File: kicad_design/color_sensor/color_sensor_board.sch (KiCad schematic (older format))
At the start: 5 parts, among them P1 CONN_6X2, P2 CONN_2, P3 CONN_2, U1 TCS3200

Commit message: Created new version 1.1 of the color sensor PCB. New version has a 5x2 header replacing the 6x2 header. Routed the shield board and re-routed sensor v1.1. Created gerber files.
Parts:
- removed P1: CONN_6X2, symbol CONN_6X2
- added P1: CONN_5X2, symbol CONN_5X2
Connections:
- net 5V: now also P1.1
- net GND: now also P1.3
- net A0 renamed S0
- net S0: now also P1.5
- net A1 renamed BLUE
- net BLUE: now also P1.6
- net A2 renamed GREEN
- net GREEN: now also P1.4
- net A3 renamed RED
- net RED: now also P1.2
- net D2 renamed FREQ
- net FREQ: now also P1.8
- net D3 renamed S2
- net S2: now also P1.9
- net D4 renamed S3
- net S3: now also P1.10
- net D5 renamed S1
- net S1: now also P1.7
- no-connect marks 2 -> 0
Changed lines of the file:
@@
-EESchema Schematic File Version 2  date Fri 21 Oct 2011 11:27:30 AM PDT
+EESchema Schematic File Version 2  date Tue 10 Jan 2012 01:09:11 PM PST
 LIBS:power
 LIBS:device
@@
 Sheet 1 1
 Title ""
-Date "21 oct 2011"
+Date "10 jan 2012"
 Rev ""
 Comp ""
@@
 Comment4 ""
 $EndDescr
-Text Label 5300 4400 2    60   ~ 0
-A3
-Text Label 5300 4300 2    60   ~ 0
-A2
-Text Label 5300 4200 2    60   ~ 0
-A1
-Wire Wire Line
-	4950 4400 5300 4400
-Wire Wire Line
-	4950 4200 5300 4200
+Text Label 5250 4050 2    60   ~ 0
+RED
+Text Label 5250 4150 2    60   ~ 0
+GREEN
+Text Label 5250 4250 2    60   ~ 0
+BLUE
+Text Label 5250 4350 2    60   ~ 0
+FREQ
+Text Label 5250 4450 2    60   ~ 0
+S3
+Text Label 3750 4450 0    60   ~ 0
+S2
+Text Label 3750 4350 0    60   ~ 0
+S1
+Text Label 3750 4250 0    60   ~ 0
+S0
+Text Label 3750 4150 0    60   ~ 0
+GND
+Text Label 3750 4050 0    60   ~ 0
+5V
+Wire Wire Line
+	4100 4450 3750 4450
+Wire Wire Line
+	4100 4250 3750 4250
+Wire Wire Line
+	4100 4050 3750 4050
+Wire Wire Line
+	4900 4350 5250 4350
+Wire Wire Line
+	4900 4150 5250 4150
 Wire Wire Line
 	6250 3950 5950 3950
 Wire Wire Line
 	3650 2550 3650 2650
-Wire Wire Line
-	4950 4000 5300 4000
-Wire Wire Line
-	4150 4400 3800 4400
-Wire Wire Line
-	4150 4200 3800 4200
 Wire Wire Line
 	8900 4400 9400 4400
@@
 Connection ~ 7550 4400
 Wire Wire Line
-	4150 4000 3800 4000
-Wire Wire Line
-	4150 4300 3800 4300
-Wire Wire Line
-	4950 3900 5300 3900
-Wire Wire Line
-	4950 4100 5300 4100
-Wire Wire Line
 	5950 4300 6250 4300
 Wire Wire Line
@@
 	6250 4150 5950 4150
 Wire Wire Line
-	4950 4300 5300 4300
+	4900 4050 5250 4050
+Wire Wire Line
+	4900 4250 5250 4250
+Wire Wire Line
+	4900 4450 5250 4450
+Wire Wire Line
+	4100 4150 3750 4150
+Wire Wire Line
+	4100 4350 3750 4350
+$Comp
+L CONN_5X2 P1
+U 1 1 4F0CA3A1
+P 4500 4250
+F 0 "P1" H 4500 4550 60  0000 C CNN
+F 1 "CONN_5X2" V 4500 4250 50  0000 C CNN
+	1    4500 4250
+	1    0    0    -1
+$EndComp
 Text Label 5950 4150 0    60   ~ 0
-A2
+GREEN
 Text Label 5950 3950 0    60   ~ 0
-A1
+BLUE
 $Comp
 L CONN_2 P3
@@
 $EndComp
 Text Label 5950 4300 0    60   ~ 0
-A3
+RED
 Text Label 5950 4500 0    60   ~ 0
 GND
@@
 	1    0    0    -1
 $EndComp
-NoConn ~ 4150 4100
-NoConn ~ 4150 3900
-Text Label 5300 4100 2    60   ~ 0
-A0
-Text Label 5300 4000 2    60   ~ 0
-D5
-Text Label 5300 3900 2    60   ~ 0
-D4
-Text Label 3800 4400 0    60   ~ 0
-D3
-Text Label 3800 4300 0    60   ~ 0
-D2
-Text Label 3800 4200 0    60   ~ 0
-GND
-Text Label 3800 4000 0    60   ~ 0
-5V
 Text Label 7300 3950 0    60   ~ 0
-A0
+S0
 Text Label 7300 4100 0    60   ~ 0
-D5
+S1
 Text Label 9400 3950 2    60   ~ 0
-D4
+S3
 Text Label 9400 4100 2    60   ~ 0
-D3
+S2
 Text Label 7550 4800 2    60   ~ 0
 GND
@@
 $EndComp
 Text Label 9400 4250 2    60   ~ 0
-D2
+FREQ
 Text Label 9400 4400 2    60   ~ 0
 5V
 $Comp
-L CONN_6X2 P1
-U 1 1 4E9F289F
-P 4550 4150
-F 0 "P1" H 4550 4500 60  0000 C CNN
-F 1 "CONN_6X2" V 4550 4150 60  0000 C CNN
-	1    4550 4150
-	1    0    0    -1
-$EndComp
-$Comp
 L TCS3200 U1

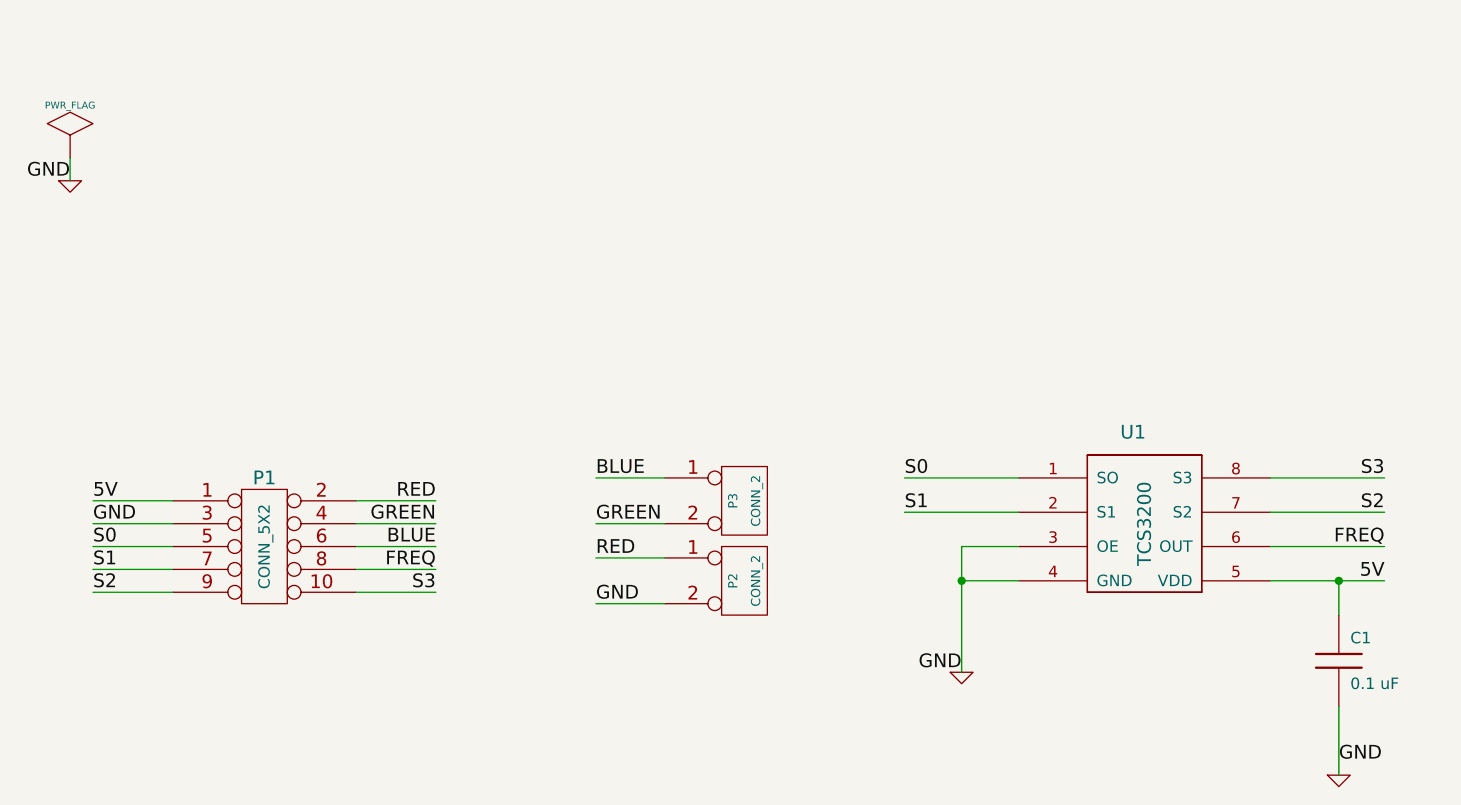
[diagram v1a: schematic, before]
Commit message: Changes to the sensor and LED boards to replace the terminal blocks with surface mount components.
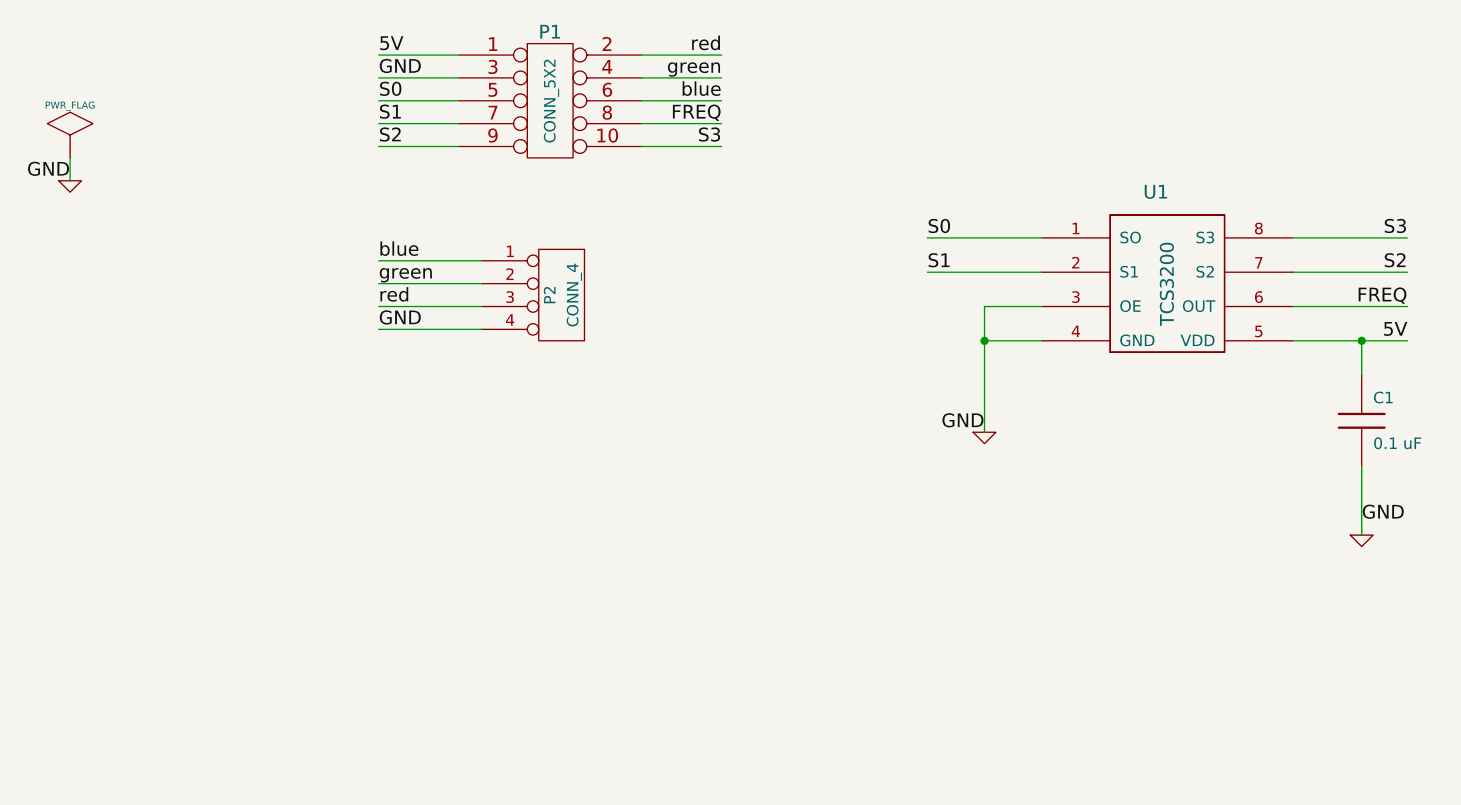
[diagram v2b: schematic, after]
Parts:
- removed P2, P3: CONN_2, symbol CONN_2
- added P2: CONN_4, symbol CONN_4
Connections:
- net GND: now also P2.4 (P4)
- net BLUE renamed blue
- net blue: now also P2.1 (P1)
- net GREEN renamed green
- net green: now also P2.2 (P2)
- net RED renamed red
- net red: now also P2.3 (P3)
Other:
- moved on the sheet: C1, P1, U1
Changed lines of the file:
@@
-EESchema Schematic File Version 2  date Tue 10 Jan 2012 01:09:11 PM PST
+EESchema Schematic File Version 2  date Thu 09 Feb 2012 05:50:30 PM PST
 LIBS:power
 LIBS:device
@@
 Sheet 1 1
 Title ""
-Date "10 jan 2012"
+Date "10 feb 2012"
 Rev ""
 Comp ""
@@
 Comment4 ""
 $EndDescr
-Text Label 5250 4050 2    60   ~ 0
-RED
-Text Label 5250 4150 2    60   ~ 0
-GREEN
-Text Label 5250 4250 2    60   ~ 0
-BLUE
-Text Label 5250 4350 2    60   ~ 0
+Text Label 5000 3300 0    60   ~ 0
+GND
+Text Label 5000 3200 0    60   ~ 0
+red
+Text Label 5000 3100 0    60   ~ 0
+green
+Text Label 5000 3000 0    60   ~ 0
+blue
+Wire Wire Line
+	5450 3300 5000 3300
+Wire Wire Line
+	5450 3100 5000 3100
+Wire Wire Line
+	5350 2500 5000 2500
+Wire Wire Line
+	5350 2300 5000 2300
+Wire Wire Line
+	5350 2100 5000 2100
+Wire Wire Line
+	6150 2400 6500 2400
+Wire Wire Line
+	6150 2200 6500 2200
+Wire Wire Line
+	3650 2550 3650 2650
+Wire Wire Line
+	9000 3350 9500 3350
+Wire Wire Line
+	7650 3350 7900 3350
+Wire Wire Line
+	7900 3200 7650 3200
+Wire Wire Line
+	9000 2900 9500 2900
+Wire Wire Line
+	9300 3900 9300 4200
+Wire Wire Line
+	7900 2900 7400 2900
+Wire Wire Line
+	9000 3200 9500 3200
+Wire Wire Line
+	9300 3500 9300 3350
+Connection ~ 9300 3350
+Wire Wire Line
+	7900 3050 7400 3050
+Wire Wire Line
+	9000 3050 9500 3050
+Wire Wire Line
+	7650 3200 7650 3750
+Connection ~ 7650 3350
+Wire Wire Line
+	6150 2100 6500 2100
+Wire Wire Line
+	6150 2300 6500 2300
+Wire Wire Line
+	6150 2500 6500 2500
+Wire Wire Line
+	5350 2200 5000 2200
+Wire Wire Line
+	5350 2400 5000 2400
+Wire Wire Line
+	5450 3000 5000 3000
+Wire Wire Line
+	5450 3200 5000 3200
+$Comp
+L CONN_4 P2
+U 1 1 4F347703
+P 5800 3150
+F 0 "P2" V 5750 3150 50  0000 C CNN
+F 1 "CONN_4" V 5850 3150 50  0000 C CNN
+	1    5800 3150
+	1    0    0    -1
+$EndComp
+Text Label 6500 2100 2    60   ~ 0
+red
+Text Label 6500 2200 2    60   ~ 0
+green
+Text Label 6500 2300 2    60   ~ 0
+blue
+Text Label 6500 2400 2    60   ~ 0
 FREQ
-Text Label 5250 4450 2    60   ~ 0
+Text Label 6500 2500 2    60   ~ 0
 S3
-Text Label 3750 4450 0    60   ~ 0
+Text Label 5000 2500 0    60   ~ 0
 S2
-Text Label 3750 4350 0    60   ~ 0
+Text Label 5000 2400 0    60   ~ 0
 S1
-Text Label 3750 4250 0    60   ~ 0
+Text Label 5000 2300 0    60   ~ 0
 S0
-Text Label 3750 4150 0    60   ~ 0
-GND
-Text Label 3750 4050 0    60   ~ 0
+Text Label 5000 2200 0    60   ~ 0
+GND
+Text Label 5000 2100 0    60   ~ 0
 5V
-Wire Wire Line
-	4100 4450 3750 4450
-Wire Wire Line
-	4100 4250 3750 4250
-Wire Wire Line
-	4100 4050 3750 4050
-Wire Wire Line
-	4900 4350 5250 4350
-Wire Wire Line
-	4900 4150 5250 4150
-Wire Wire Line
-	6250 3950 5950 3950
-Wire Wire Line
-	3650 2550 3650 2650
-Wire Wire Line
-	8900 4400 9400 4400
-Wire Wire Line
-	7550 4400 7800 4400
-Wire Wire Line
-	7800 4250 7550 4250
-Wire Wire Line
-	8900 3950 9400 3950
-Wire Wire Line
-	9200 4950 9200 5250
-Wire Wire Line
-	7800 3950 7300 3950
-Wire Wire Line
-	8900 4250 9400 4250
-Wire Wire Line
-	9200 4550 9200 4400
-Connection ~ 9200 4400
-Wire Wire Line
-	7800 4100 7300 4100
-Wire Wire Line
-	8900 4100 9400 4100
-Wire Wire Line
-	7550 4250 7550 4800
-Connection ~ 7550 4400
-Wire Wire Line
-	5950 4300 6250 4300
-Wire Wire Line
-	6250 4500 5950 4500
-Wire Wire Line
-	6250 4150 5950 4150
-Wire Wire Line
-	4900 4050 5250 4050
-Wire Wire Line
-	4900 4250 5250 4250
-Wire Wire Line
-	4900 4450 5250 4450
-Wire Wire Line
-	4100 4150 3750 4150
-Wire Wire Line
-	4100 4350 3750 4350
 $Comp
 L CONN_5X2 P1
 U 1 1 4F0CA3A1
-P 4500 4250
-F 0 "P1" H 4500 4550 60  0000 C CNN
-F 1 "CONN_5X2" V 4500 4250 50  0000 C CNN
-	1    4500 4250
-	1    0    0    -1
-$EndComp
-Text Label 5950 4150 0    60   ~ 0
-GREEN
-Text Label 5950 3950 0    60   ~ 0
-BLUE
-$Comp
-L CONN_2 P3
-U 1 1 4EA0C6DF
-P 6600 4050
-F 0 "P3" V 6550 4050 40  0000 C CNN
-F 1 "CONN_2" V 6650 4050 40  0000 C CNN
-	1    6600 4050
-	1    0    0    -1
-$EndComp
-Text Label 5950 4300 0    60   ~ 0
-RED
-Text Label 5950 4500 0    60   ~ 0
-GND
-$Comp
-L CONN_2 P2
-U 1 1 4E9F77B0
-P 6600 4400
-F 0 "P2" V 6550 4400 40  0000 C CNN
-F 1 "CONN_2" V 6650 4400 40  0000 C CNN
-	1    6600 4400
+P 5750 2300
+F 0 "P1" H 5750 2600 60  0000 C CNN
+F 1 "CONN_5X2" V 5750 2300 50  0000 C CNN
+	1    5750 2300
 	1    0    0    -1
 $EndComp
@@
 	1    0    0    -1
 $EndComp
-Text Label 7300 3950 0    60   ~ 0
+Text Label 7400 2900 0    60   ~ 0
 S0
-Text Label 7300 4100 0    60   ~ 0
+Text Label 7400 3050 0    60   ~ 0
 S1
-Text Label 9400 3950 2    60   ~ 0
+Text Label 9500 2900 2    60   ~ 0
 S3
-Text Label 9400 4100 2    60   ~ 0
+Text Label 9500 3050 2    60   ~ 0
 S2
-Text Label 7550 4800 2    60   ~ 0
+Text Label 7650 3750 2    60   ~ 0
 GND
 $Comp
 L GND #PWR03
 U 1 1 4E9F2B4B
-P 7550 4800
-F 0 "#PWR03" H 7550 4800 30  0001 C CNN
-F 1 "GND" H 7550 4730 30  0001 C CNN
-	1    7550 4800
-	1    0    0    -1
-$EndComp
-Text Label 9200 5200 0    60   ~ 0
+P 7650 3750
+F 0 "#PWR03" H 7650 3750 30  0001 C CNN
+F 1 "GND" H 7650 3680 30  0001 C CNN
+	1    7650 3750
+	1    0    0    -1
+$EndComp
+Text Label 9300 4150 0    60   ~ 0
 GND
 $Comp
 L GND #PWR04
 U 1 1 4E9F2A66
-P 9200 5250
-F 0 "#PWR04" H 9200 5250 30  0001 C CNN
-F 1 "GND" H 9200 5180 30  0001 C CNN
-	1    9200 5250
+P 9300 4200
+F 0 "#PWR04" H 9300 4200 30  0001 C CNN
+F 1 "GND" H 9300 4130 30  0001 C CNN
+	1    9300 4200
 	1    0    0    -1
 $EndComp
@@
 L C C1
 U 1 1 4E9F2A04
-P 9200 4750
-F 0 "C1" H 9250 4850 50  0000 L CNN
-F 1 "0.1 uF" H 9250 4650 50  0000 L CNN
-	1    9200 4750
-	1    0    0    -1
-$EndComp
-Text Label 9400 4250 2    60   ~ 0
+P 9300 3700
+F 0 "C1" H 9350 3800 50  0000 L CNN
+F 1 "0.1 uF" H 9350 3600 50  0000 L CNN
+	1    9300 3700
+	1    0    0    -1
+$EndComp
+Text Label 9500 3200 2    60   ~ 0
 FREQ
-Text Label 9400 4400 2    60   ~ 0
+Text Label 9500 3350 2    60   ~ 0
 5V
 $Comp
 L TCS3200 U1
 U 1 1 4E9F1F08
-P 7750 5050
-F 0 "U1" H 8300 6350 60  0000 C CNN
-F 1 "TCS3200" V 8350 5950 60  0000 C CNN
-	1    7750 5050
-	1    0    0    -1
-$EndComp
+P 7850 4000
+F 0 "U1" H 8400 5300 60  0000 C CNN
+F 1 "TCS3200" V 8450 4900 60  0000 C CNN
+	1    7850 4000
+	1    0    0    -1
+$EndComp
